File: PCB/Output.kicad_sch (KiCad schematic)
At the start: 34 parts, among them J4 Headphone Output, J5 BNC Output, Q1 2N7002, Q2 2N7002, U3 SFH617A-1, U4 HFBR-1412PTZ

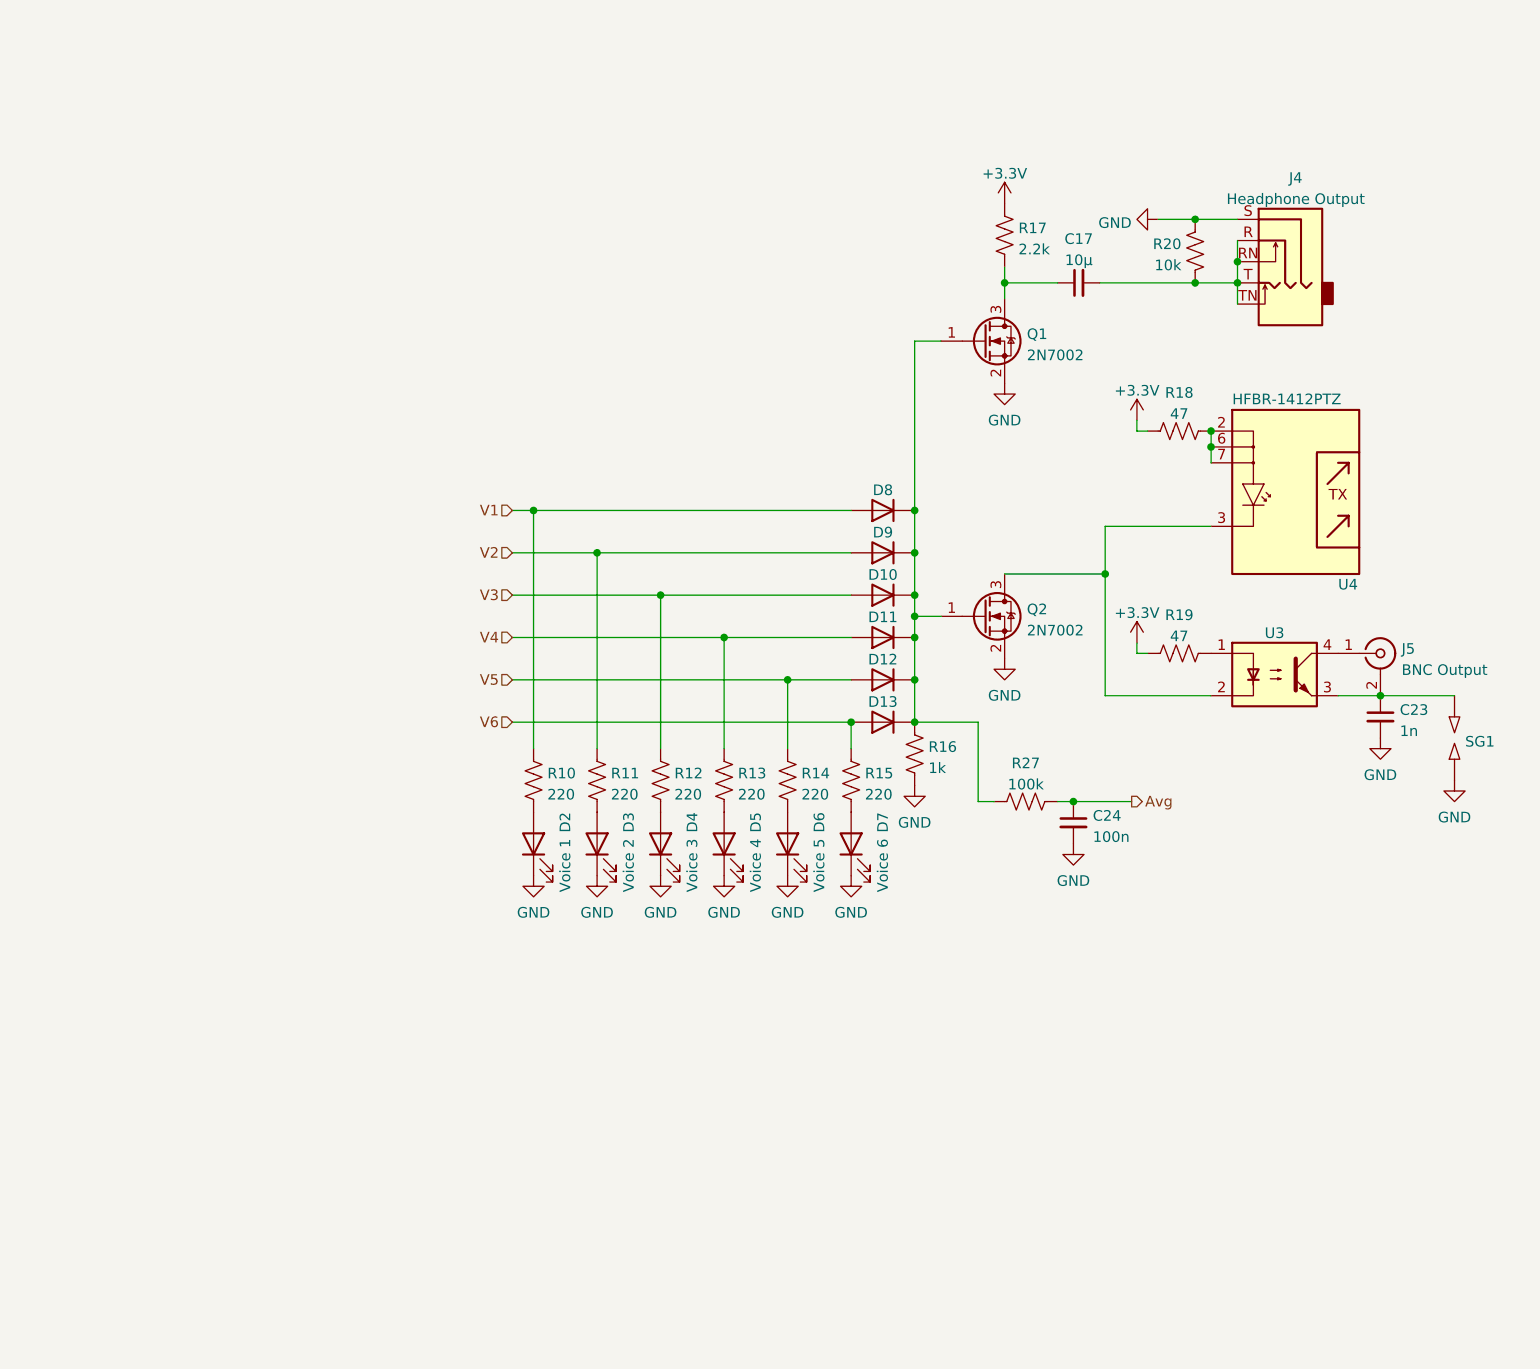
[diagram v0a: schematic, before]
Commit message: fixed PCB
 * Added 5.1k resistors to CC lines on USB-C port
 * Replaced diode OR thing and MOSFET with too low of a threshold voltage with a real OR gate and buffer
 * Fixed polarity of BNC output
 * Made headphone output not murderously loud and asymmetric
 * Added direct in/out to expansion pins
 * Reduced impedance into ADC for average volume level sensing
 * Increased MIDI input pullup resistance
 * Made thermal spokes to copper planes thinner
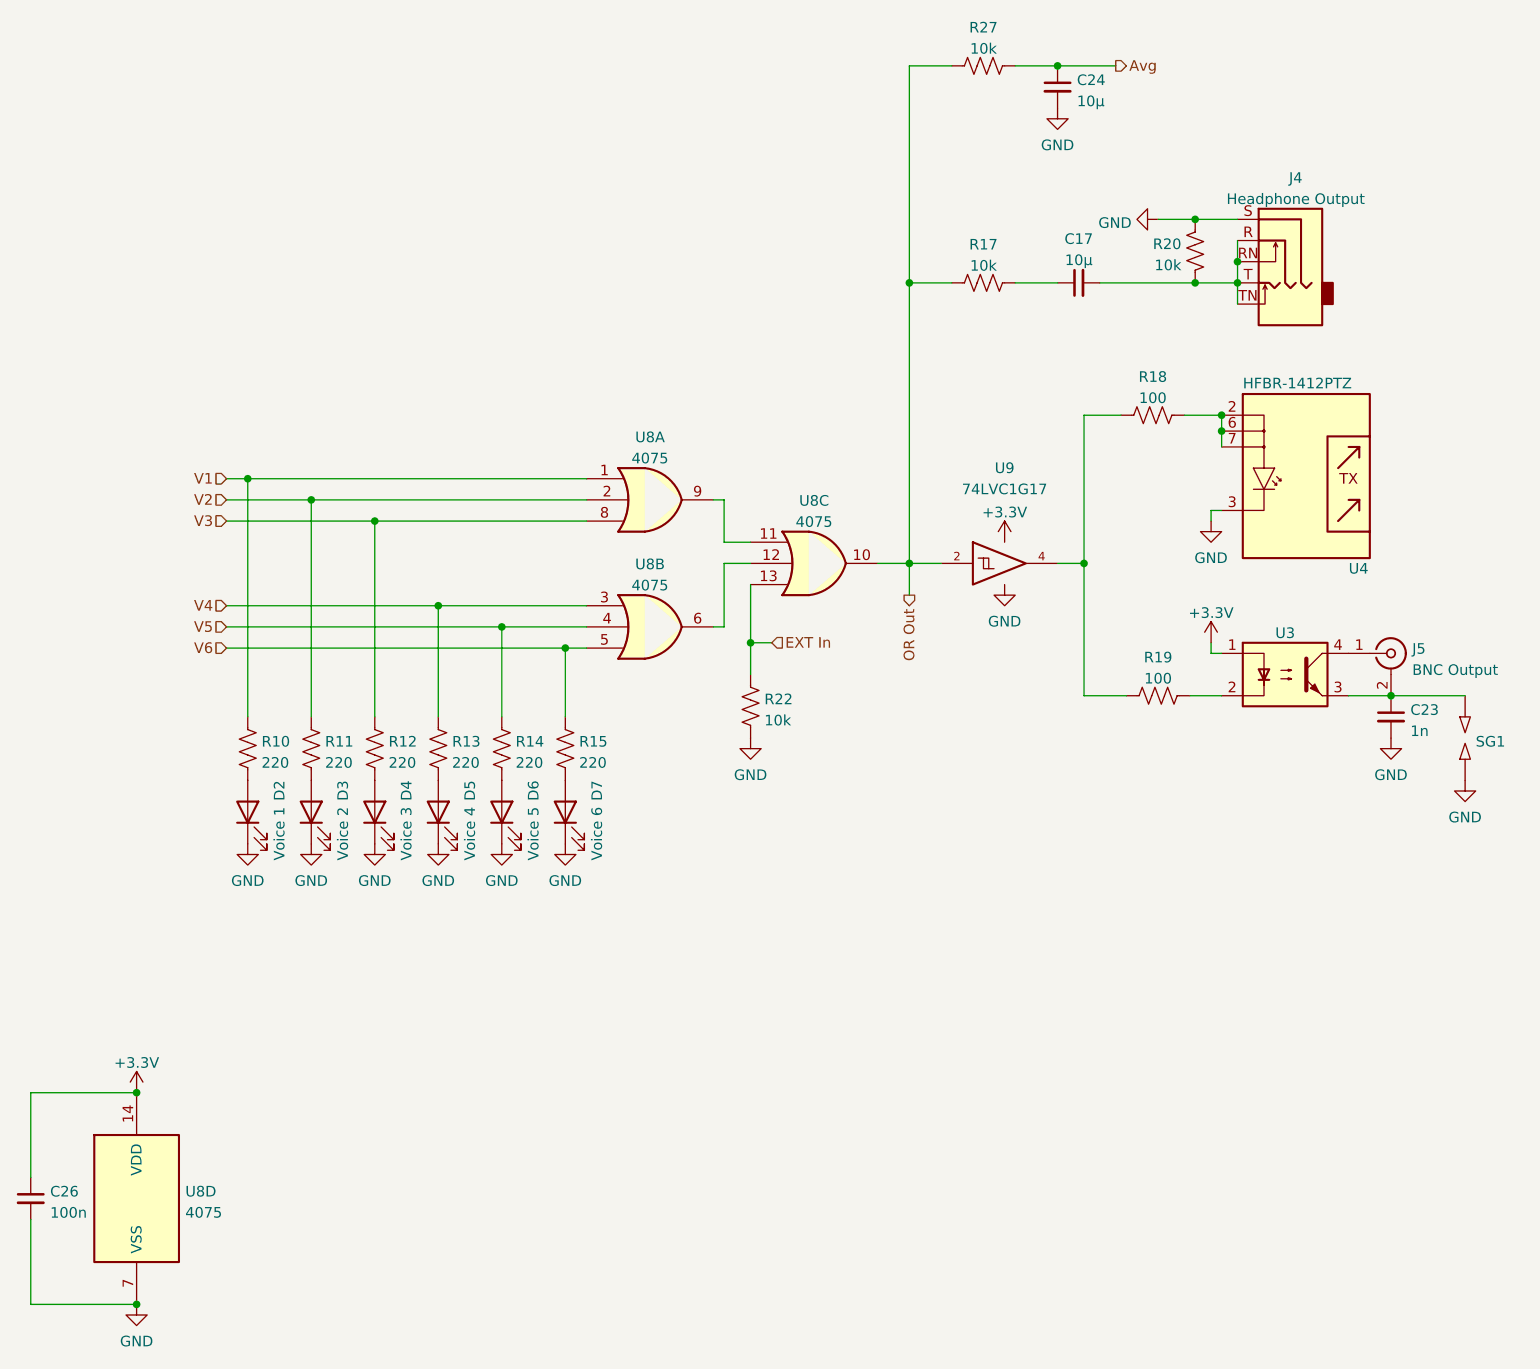
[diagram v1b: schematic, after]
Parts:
- removed D10, D11, D12, D13, D8, D9: D, Diode_SMD:D_SOD-123, symbol Device:D
- removed Q1, Q2: 2N7002, Package_TO_SOT_SMD:SOT-23, symbol Device:Q_NMOS_GSD
- removed R16: 1k, Resistor_SMD:R_0603_1608Metric_Pad0.98x0.95mm_HandSolder, symbol Device:R_US
- added C26: 100n, Capacitor_SMD:C_0603_1608Metric_Pad1.08x0.95mm_HandSolder, symbol Device:C_Small
- added R22: 10k, Resistor_SMD:R_0603_1608Metric_Pad0.98x0.95mm_HandSolder, symbol Device:R_US
- added U8: 4075, Package_SO:SOIC-14_3.9x8.7mm_P1.27mm, symbol 4xxx:4075
- added U9: 74LVC1G17, Package_TO_SOT_SMD:SOT-23-5, symbol 74xGxx:74LVC1G17
- C24: value 100n -> 10µ; footprint Capacitor_SMD:C_0603_1608Metric_Pad1.08x0.95mm_HandSolder -> Capacitor_SMD:C_0805_2012Metric_Pad1.18x1.45mm_HandSolder
- R17: value 2.2k -> 10k
- R18, R19: value 47 -> 100
- R27: value 100k -> 10k
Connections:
- net +3.3V: now also U3.1, C26.1, U8.14 (VDD), U9.5 (VCC); no longer R17.1, R18.2, R19.2
- net GND: now also U4.3, C26.2, R22.2, U8.7 (VSS), U9.3 (GND)
- net V1: now also U8.1
- net V2: now also U8.2
- net V3: now also U8.8
- net V4: now also U8.3
- net V5: now also U8.4
- net V6: now also U8.5
- net OR Out: now reaches R27.1
- net OR Out: now also R17.1, U8.10, U9.2
- net at R19.1: now also U3.2; no longer U3.1
- new net: U8.11, U8.9
- new net: U8.12, U8.6
- new net: R18.2, R19.2, U9.4
- new net EXT In: R22.1, U8.13
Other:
- moved on the sheet: C23, C24, D2, D3, D4, D5, D6, D7, J5, R10, R11, R12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
